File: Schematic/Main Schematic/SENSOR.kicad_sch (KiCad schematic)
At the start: 11 parts, among them IC2 LM75AD,118

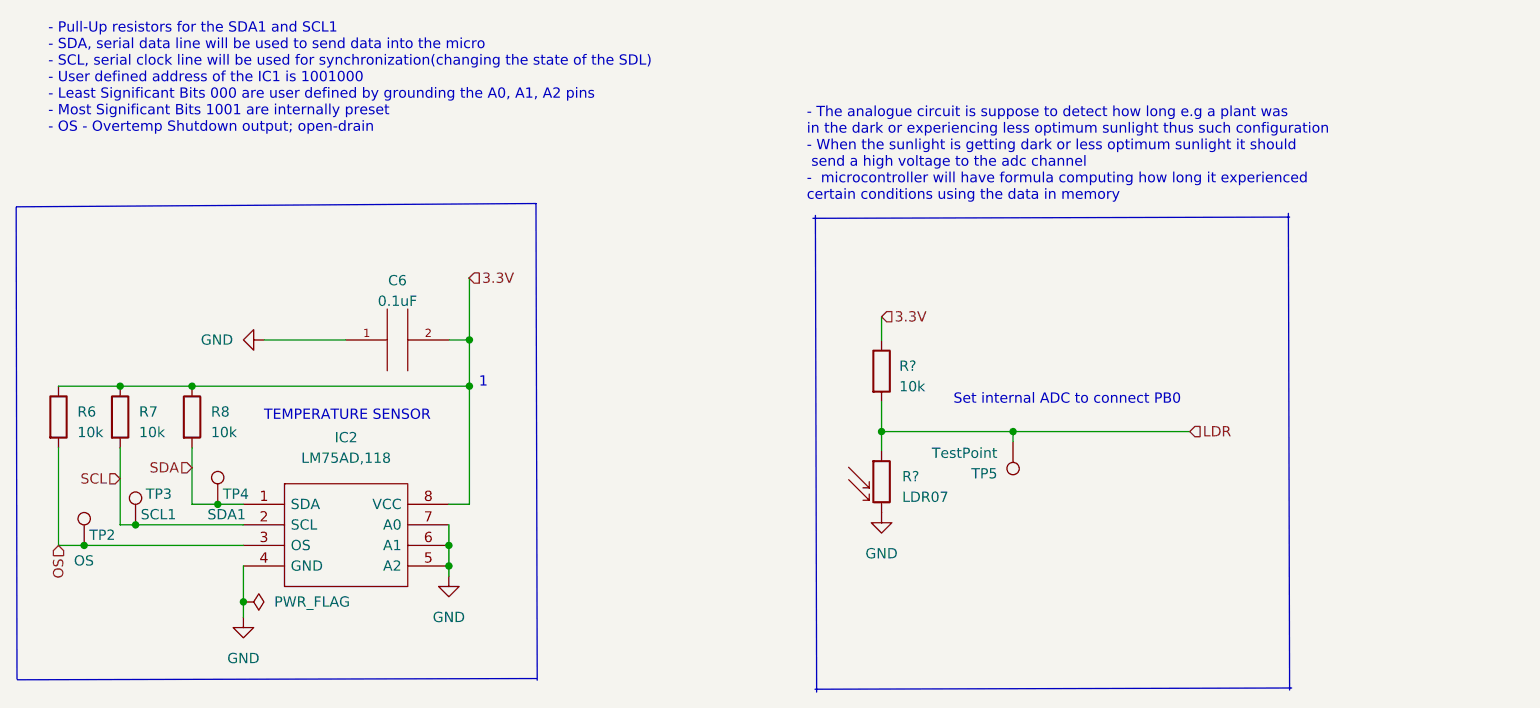
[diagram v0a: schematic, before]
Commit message: Footprints all added and the PCB has been created but not placed according to the proper configuration
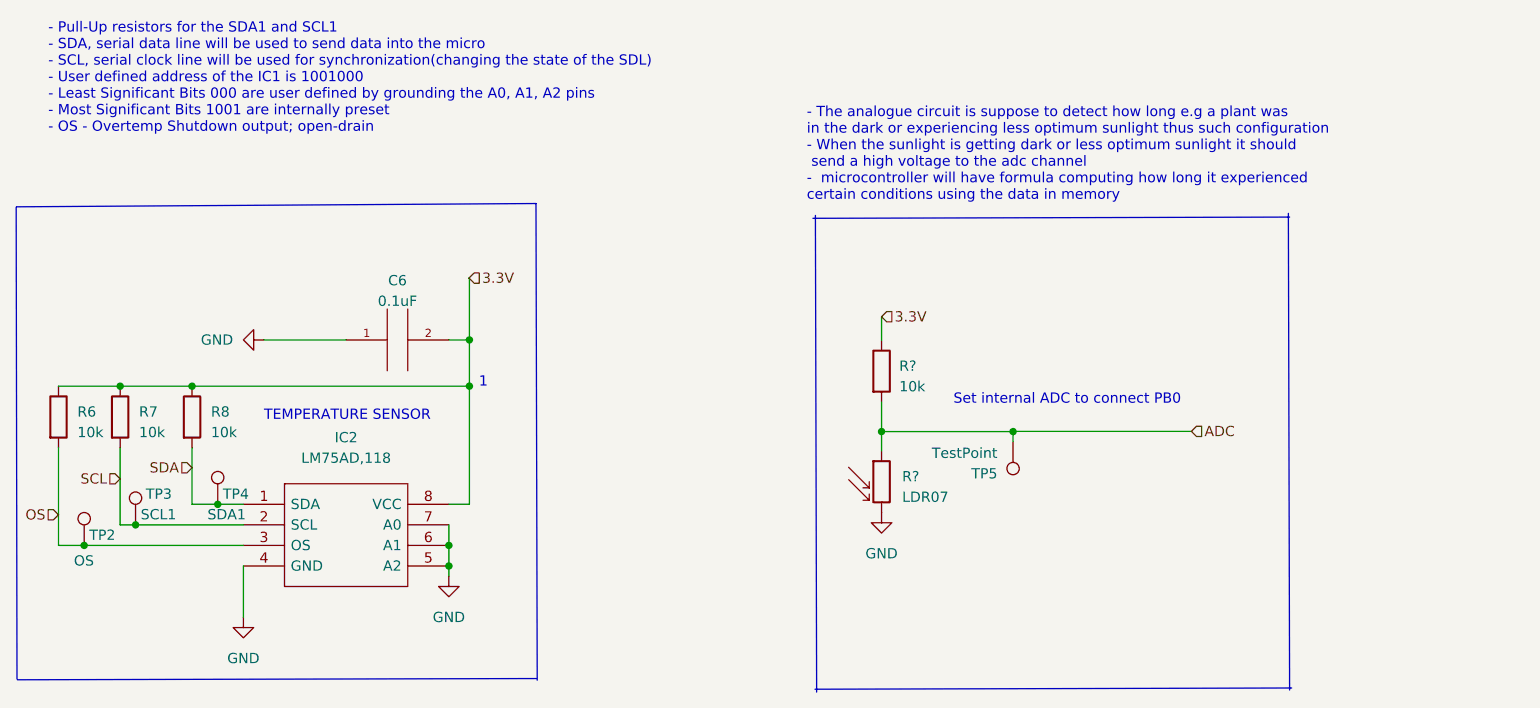
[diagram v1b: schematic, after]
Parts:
- C6: footprint CAP_10NF:CAPC1005X55N -> A_New_folder:C1206
- IC2: footprint LM75AD:SOIC127P600X175-8N -> A_New_folder:SOIC-8_L5.0-W4.0-P1.27-LS6.0-BL
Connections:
- net LDR renamed ADC
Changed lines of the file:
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@@
   (junction (at 65.6082 125.4506) (diameter 0) (color 0 0 0 0)
   )
-  (junction (at 85.2932 132.4356) (diameter 0) (color 0 0 0 0)
-  )
   (junction (at 70.0532 105.7656) (diameter 0) (color 0 0 0 0)
   )
@@
     (stroke (width 0) (type default))
   )
+  (wire (pts (xy 202.4888 111.3536) (xy 180.4416 111.3536))
+    (stroke (width 0) (type default))
+  )
   (wire (pts (xy 62.4332 125.4506) (xy 62.4332 113.3856))
     (stroke (width 0) (type default))
@@
     (stroke (width 0) (type default))
   )
+  (wire (pts (xy 180.4416 111.3536) (xy 180.4416 111.379))
+    (stroke (width 0) (type default))
+  )
+  (wire (pts (xy 164.1856 111.379) (xy 164.1856 113.7666))
+    (stroke (width 0) (type default))
+  )
+  (wire (pts (xy 82.1182 120.3706) (xy 78.9432 120.3706))
+    (stroke (width 0) (type default))
+  )
+  (wire (pts (xy 113.2332 105.7656) (xy 113.2332 120.3706))
+    (stroke (width 0) (type default))
+  )
+  (wire (pts (xy 85.2932 127.9906) (xy 85.2932 134.3406))
+    (stroke (width 0) (type default))
+  )
+  (polyline (pts (xy 155.702 85.0138) (xy 214.63 84.8614))
+    (stroke (width 0) (type default))
+  )
+  (wire (pts (xy 113.2332 92.4052) (xy 113.2332 100.0506))
+    (stroke (width 0) (type default))
+  )
+  (wire (pts (xy 70.0532 105.7656) (xy 78.9432 105.7656))
+    (stroke (width 0) (type default))
+  )
+  (polyline (pts (xy 155.956 143.2306) (xy 214.884 143.0782))
+    (stroke (width 0) (type default))
+  )
+  (polyline (pts (xy 156.0068 84.6582) (xy 156.1592 143.5862))
+    (stroke (width 0) (type default))
+  )
   (wire (pts (xy 180.4416 111.379) (xy 180.4416 112.649))
     (stroke (width 0) (type default))
   )
-  (wire (pts (xy 164.1856 111.379) (xy 164.1856 113.7666))
-    (stroke (width 0) (type default))
-  )
-  (wire (pts (xy 82.1182 120.3706) (xy 78.9432 120.3706))
-    (stroke (width 0) (type default))
-  )
-  (wire (pts (xy 113.2332 105.7656) (xy 113.2332 120.3706))
-    (stroke (width 0) (type default))
-  )
-  (wire (pts (xy 85.2932 127.9906) (xy 85.2932 132.4356))
-    (stroke (width 0) (type default))
-  )
-  (polyline (pts (xy 155.702 85.0138) (xy 214.63 84.8614))
-    (stroke (width 0) (type default))
-  )
-  (wire (pts (xy 85.2932 132.4356) (xy 85.2932 134.3406))
-    (stroke (width 0) (type default))
-  )
-  (wire (pts (xy 113.2332 92.4052) (xy 113.2332 100.0506))
-    (stroke (width 0) (type default))
-  )
-  (wire (pts (xy 70.0532 105.7656) (xy 78.9432 105.7656))
-    (stroke (width 0) (type default))
-  )
-  (polyline (pts (xy 155.956 143.2306) (xy 214.884 143.0782))
-    (stroke (width 0) (type default))
-  )
-  (polyline (pts (xy 156.0068 84.6582) (xy 156.1592 143.5862))
-    (stroke (width 0) (type default))
-  )
   (wire (pts (xy 110.6932 125.4506) (xy 110.6932 127.9906))
     (stroke (width 0) (type default))
@@
   )
   (wire (pts (xy 65.6082 125.4506) (xy 85.2932 125.4506))
-    (stroke (width 0) (type default))
-  )
-  (wire (pts (xy 180.4416 111.379) (xy 202.2856 111.379))
     (stroke (width 0) (type default))
   )
@@
     (effects (font (size 1.27 1.27)) (justify left))
   )
-  (hierarchical_label "LDR" (shape input) (at 202.2856 111.379 0) (fields_autoplaced)
+  (hierarchical_label "ADC" (shape input) (at 202.4888 111.3536 0) (fields_autoplaced)
     (effects (font (size 1.27 1.27)) (justify left))
   )
-  (hierarchical_label "OS" (shape input) (at 62.4332 125.4506 270) (fields_autoplaced)
+  (hierarchical_label "OS" (shape input) (at 62.4332 121.666 180) (fields_autoplaced)
     (effects (font (size 1.27 1.27)) (justify right))
   )
@@
     )
   )
-  (symbol (lib_id "power:PWR_FLAG") (at 85.2932 132.4356 270) (unit 1)
-    (in_bom yes) (on_board yes) (dnp no) (fields_autoplaced)
-    (property "Reference" "#FLG03" (at 87.1982 132.4356 0)
-      (effects (font (size 1.27 1.27)) hide)
-    )
-    (property "Value" "PWR_FLAG" (at 89.1032 132.4355 90)
-      (effects (font (size 1.27 1.27)) (justify left))
-    )
-    (property "Footprint" "" (at 85.2932 132.4356 0)
-      (effects (font (size 1.27 1.27)) hide)
-    )
-    (property "Datasheet" "~" (at 85.2932 132.4356 0)
-      (effects (font (size 1.27 1.27)) hide)
-    )
-    (pin "1")
-    (instances
-      (project "Main Schematic"
-        (path "/81c41bad-bb43-41af-b405-18d135a809b1/820a1ce6-42c1-4792-8ad0-5e2a5c074ed4"
-          (reference "#FLG03") (unit 1)
-        )
-      )
-      (project "sensing"
-        (path "/ae78189d-79c7-41a0-b77c-3bb766898352"
-          (reference "#FLG?") (unit 1)
-        )
-      )
-    )
-  )
   (symbol (lib_id "LM75:LM75AD,118") (at 85.2932 120.3706 0) (unit 1)
     (in_bom yes) (on_board yes) (dnp no) (fields_autoplaced)
@@
       (effects (font (size 1.27 1.27)))
     )
-    (property "Footprint" "LM75AD:SOIC127P600X175-8N" (at 106.8832 117.8306 0)
+    (property "Footprint" "A_New_folder:SOIC-8_L5.0-W4.0-P1.27-LS6.0-BL" (at 106.8832 117.8306 0)
       (effects (font (size 1.27 1.27)) (justify left) hide)
     )
@@
       (effects (font (size 1.27 1.27)))
     )
-    (property "Footprint" "CAP_10NF:CAPC1005X55N" (at 104.3432 100.0506 0)
-      (effects (font (size 1.27 1.27)) hide)
-    )
+    (property "Footprint" "A_New_folder:C1206" (at 104.3432 100.0506 0)
+      (effects (font (size 1.27 1.27)) hide)
+    )

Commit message: Update
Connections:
- net SDA renamed SDL
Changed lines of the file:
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@@
     (effects (font (size 1.27 1.27)) (justify right))
   )
-  (hierarchical_label "SDA" (shape input) (at 78.9432 115.8494 180) (fields_autoplaced)
+  (hierarchical_label "SDL" (shape input) (at 78.9432 115.8494 180) (fields_autoplaced)
     (effects (font (size 1.27 1.27)) (justify right))
   )

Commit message: I've added the local footprints and gerber files into the repo
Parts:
- C6: footprint A_New_folder:C1206 -> Local_Footprints:C1206
- IC2: footprint A_New_folder:SOIC-8_L5.0-W4.0-P1.27-LS6.0-BL -> Local_Footprints:SOIC-8_L5.0-W4.0-P1.27-LS6.0-BL
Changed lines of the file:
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@@
       (effects (font (size 1.27 1.27)))
     )
-    (property "Footprint" "A_New_folder:SOIC-8_L5.0-W4.0-P1.27-LS6.0-BL" (at 106.8832 117.8306 0)
+    (property "Footprint" "Local_Footprints:SOIC-8_L5.0-W4.0-P1.27-LS6.0-BL" (at 106.8832 117.8306 0)
       (effects (font (size 1.27 1.27)) (justify left) hide)
     )
@@
       (effects (font (size 1.27 1.27)))
     )
-    (property "Footprint" "A_New_folder:C1206" (at 104.3432 100.0506 0)
-      (effects (font (size 1.27 1.27)) hide)
-    )
+    (property "Footprint" "Local_Footprints:C1206" (at 104.3432 100.0506 0)
+      (effects (font (size 1.27 1.27)) hide)
+    )

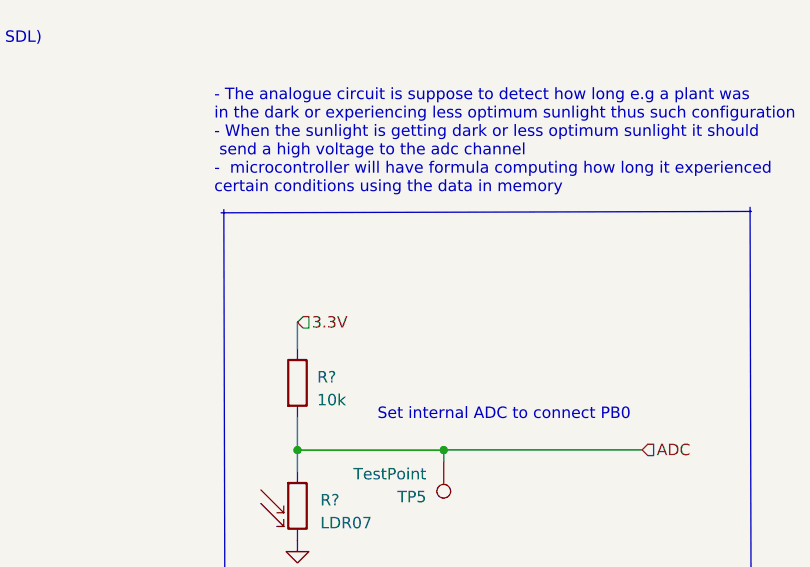
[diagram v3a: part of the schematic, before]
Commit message: Added conn for sensor
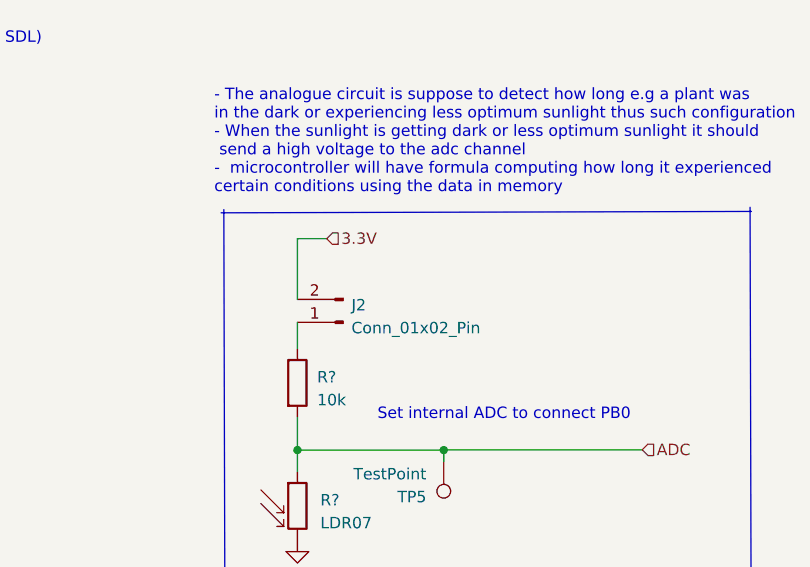
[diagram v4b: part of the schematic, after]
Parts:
- added J2: Conn_01x02_Pin, Connector_PinHeader_2.54mm:PinHeader_1x02_P2.54mm_Vertical, symbol Connector:Conn_01x02_Pin
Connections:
- net 3.3V: now also J2.2 (Pin_2); no longer R?.1
- new net: J2.1 (Pin_1), R?.1
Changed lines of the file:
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@@
+    (stroke (width 0) (type default))
+  )
+  (wire (pts (xy 164.1856 94.6404) (xy 164.1856 87.884))
     (stroke (width 0) (type default))
   )
@@
   )
   (wire (pts (xy 110.6932 127.9906) (xy 110.6932 129.2606))
+    (stroke (width 0) (type default))
+  )
+  (wire (pts (xy 164.1856 87.884) (xy 167.4368 87.884))
     (stroke (width 0) (type default))
   )
@@
     (effects (font (size 1.27 1.27)) (justify left bottom))
   )
-  (hierarchical_label "3.3V" (shape input) (at 164.1856 97.1804 0) (fields_autoplaced)
+  (hierarchical_label "3.3V" (shape input) (at 167.4368 87.884 0) (fields_autoplaced)
     (effects (font (size 1.27 1.27)) (justify left))
   )
@@
     (effects (font (size 1.27 1.27)) (justify left))
   )
+  (symbol (lib_id "Connector:Conn_01x02_Pin") (at 169.2656 97.1804 180) (unit 1)
+    (in_bom yes) (on_board yes) (dnp no) (fields_autoplaced)
+    (property "Reference" "J2" (at 170.18 95.2754 0)
+      (effects (font (size 1.27 1.27)) (justify right))
+    )
+    (property "Value" "Conn_01x02_Pin" (at 170.18 97.8154 0)
+      (effects (font (size 1.27 1.27)) (justify right))
+    )
+    (property "Footprint" "Connector_PinHeader_2.54mm:PinHeader_1x02_P2.54mm_Vertical" (at 169.2656 97.1804 0)
+      (effects (font (size 1.27 1.27)) hide)
+    )
+    (property "Datasheet" "~" (at 169.2656 97.1804 0)
+      (effects (font (size 1.27 1.27)) hide)
+    )
+    (pin "1")
+    (pin "2")
+    (instances
+      (project "Main Schematic"
+        (path "/81c41bad-bb43-41af-b405-18d135a809b1/820a1ce6-42c1-4792-8ad0-5e2a5c074ed4"
+          (reference "J2") (unit 1)
+        )
+      )
+    )
+  )
   (symbol (lib_id "power:GND") (at 110.6932 129.2606 0) (unit 1)

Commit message: Design part Done
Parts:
- R6, R7, R8, R?: footprint Resistor_SMD:R_1206_3216Metric -> Local_Footprints:R0805
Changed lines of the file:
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@@
       (effects (font (size 1.27 1.27)) (justify left))
     )
-    (property "Footprint" "Resistor_SMD:R_1206_3216Metric" (at 77.1652 109.5756 90)
+    (property "Footprint" "Local_Footprints:R0805" (at 77.1652 109.5756 90)
       (effects (font (size 1.27 1.27)) hide)
     )
@@
       (effects (font (size 1.27 1.27)) (justify left))
     )
-    (property "Footprint" "Resistor_SMD:R_1206_3216Metric" (at 68.2752 109.5756 90)
+    (property "Footprint" "Local_Footprints:R0805" (at 68.2752 109.5756 90)
       (effects (font (size 1.27 1.27)) hide)
     )
@@
       (effects (font (size 1.27 1.27)) (justify left))
     )
-    (property "Footprint" "Resistor_SMD:R_1206_3216Metric" (at 162.4076 103.9114 90)
+    (property "Footprint" "Local_Footprints:R0805" (at 162.4076 103.9114 90)
       (effects (font (size 1.27 1.27)) hide)
     )
@@
       (effects (font (size 1.27 1.27)) (justify left))
     )
-    (property "Footprint" "Resistor_SMD:R_1206_3216Metric" (at 60.6552 109.5756 90)
-      (effects (font (size 1.27 1.27)) hide)
-    )
+    (property "Footprint" "Local_Footprints:R0805" (at 60.6552 109.5756 90)
+      (effects (font (size 1.27 1.27)) hide)
+    )
